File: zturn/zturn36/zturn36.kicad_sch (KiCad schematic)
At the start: 61 parts, among them J11 Conn_02x40_Odd_Even, J12 Conn_02x40_Odd_Even, J5V1 Conn_01x03, Q1 SSM6N15AFU, Q2 SSM6N15AFU, Q3 SSM6N15AFU, Q4 SSM6N15AFU, Q5 SSM6N15AFU, Q6 SSM6N15AFU, Q7 SSM6N15AFU, Q8 SSM6N15AFU, Q9 SSM6N15AFU, U1 74AXP4T245, U10 74AXP4T245, U11 74AXP4T245, U12 74AXP4T245, U13 74AXP4T245, U14 LM3940_TO220, U2 74AXP4T245, U3 74AXP4T245, U8 74AXP4T245, U9 74AXP4T245

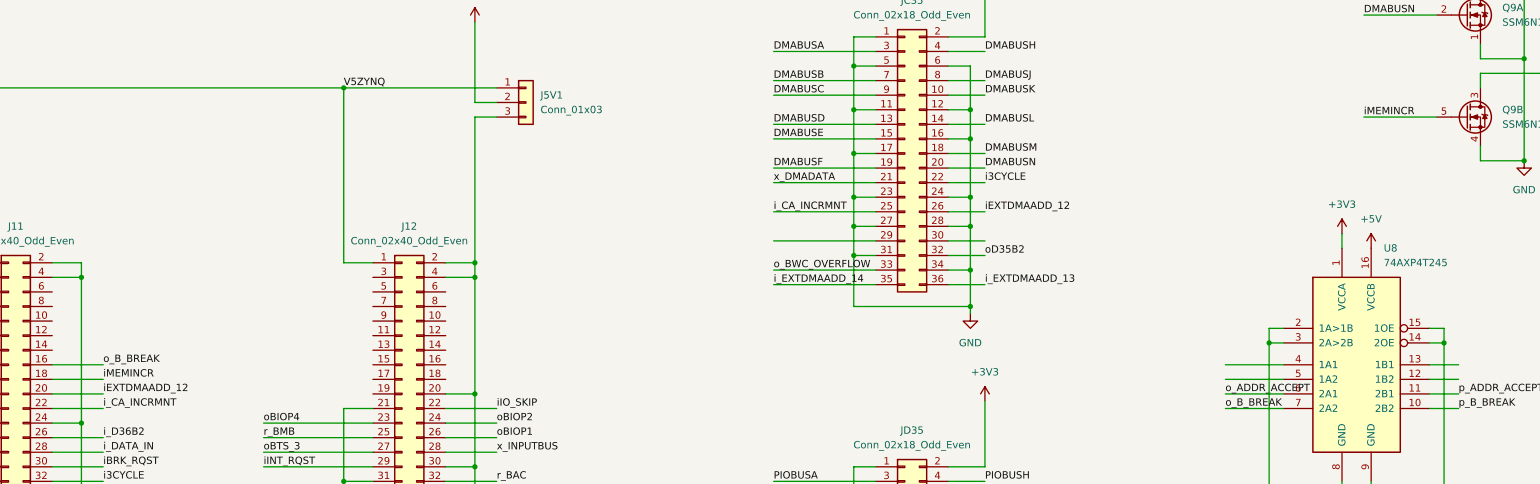
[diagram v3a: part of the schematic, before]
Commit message: fixed polarity of bus signals for the open-drain transistors
    PDP         Zynq
    MEM         _MEM
    MEM_P       _MEM_P
    _DMAADDR    DMAADDR
    _DMADATA    DMADATA
    _INPUTBUS   INPUTBUS

Also fixed MEMINCR polarity and fixed missing ground connection on circuit board.
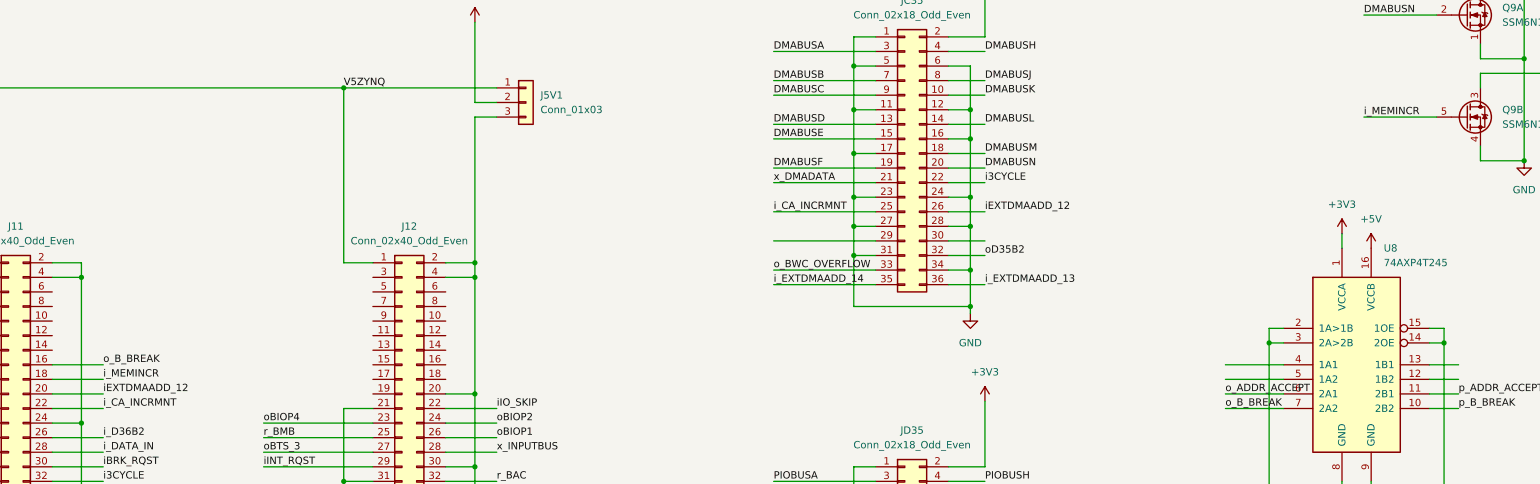
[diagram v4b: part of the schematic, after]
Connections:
- net iMEMINCR renamed i_MEMINCR
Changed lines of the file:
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@@
     (effects (font (size 1.27 1.27)) (justify left bottom))
   )
-  (label "iMEMINCR" (at 54.61 226.06 0) (fields_autoplaced)
+  (label "i_MEMINCR" (at 54.61 226.06 0) (fields_autoplaced)
     (effects (font (size 1.27 1.27)) (justify left bottom))
   )
@@
     (effects (font (size 1.27 1.27)) (justify left bottom))
   )
-  (label "iMEMINCR" (at 274.32 180.34 0) (fields_autoplaced)
+  (label "i_MEMINCR" (at 274.32 180.34 0) (fields_autoplaced)
     (effects (font (size 1.27 1.27)) (justify left bottom))
   )

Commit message: update signals and zturn pcbs with pullups
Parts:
- removed C4: 0.47u, Capacitor_SMD:C_0201_0603Metric, symbol Device:C
- removed C5: 33u, Capacitor_Tantalum_SMD:CP_EIA-7343-31_Kemet-D, symbol Device:C_Polarized_US
- removed U14: LM3940_TO220, Package_TO_SOT_THT:TO-220-3_Horizontal_TabDown, symbol Regulator_Linear:LM7805_TO220
- added R1, R2: 1K, Resistor_THT:R_Axial_DIN0204_L3.6mm_D1.6mm_P5.08mm_Horizontal, symbol Device:R_US
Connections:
- net +3V3: now also J11.3 (Pin_3), J12.3 (Pin_3)
- net +5V: now also R1.1, R2.1
- net jB36V1: now also R1.2
- net jD36B2: now also R2.2

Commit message: add I2C circuit to zturn boardset to operate front panel board
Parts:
- added JI2C1: Conn_01x03, Connector_PinHeader_2.54mm:PinHeader_1x03_P2.54mm_Horizontal, symbol Connector_Generic:Conn_01x03
- added R4: 1K, Resistor_THT:R_Axial_DIN0204_L3.6mm_D1.6mm_P5.08mm_Horizontal, symbol Device:R_US
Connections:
- net +3V3: now also U8.3 (2A>2B)
- net +5V: now also R4.1
- net GND: now also JI2C1.2 (Pin_2); no longer JC36.N2, U8.3 (2A>2B)
- net PIOBUSA: now also J11.27 (Pin_27); no longer J11.19 (Pin_19)
- net PIOBUSB: now also J11.31 (Pin_31); no longer J11.23 (Pin_23)
- net PIOBUSC: now also J11.37 (Pin_37); no longer J11.29 (Pin_29)
- net PIOBUSD: now also J12.36 (Pin_36); no longer J11.37 (Pin_37)
- net PIOBUSE: now also J12.34 (Pin_34); no longer J11.41 (Pin_41)
- net PIOBUSF: now also J12.26 (Pin_26); no longer J12.34 (Pin_34)
- net PIOBUSH: now also J11.29 (Pin_29); no longer J11.21 (Pin_21)
- net PIOBUSJ: now also J11.33 (Pin_33); no longer J11.27 (Pin_27)
- net PIOBUSK: now also J11.41 (Pin_41); no longer J11.31 (Pin_31)
- net PIOBUSL: now also J12.38 (Pin_38); no longer J11.33 (Pin_33)
- net PIOBUSM: now also J12.32 (Pin_32); no longer J12.38 (Pin_38)
- net PIOBUSN: now also J12.28 (Pin_28); no longer J12.36 (Pin_36)
- net iAC_CLEAR: now also J12.45 (Pin_45); no longer J12.35 (Pin_35)
- net iINT_RQST: now also J12.39 (Pin_39); no longer J12.29 (Pin_29)
- net iIO_SKIP: now also J12.29 (Pin_29); no longer J12.22 (Pin_22)
- net oBIOP1: now also J12.23 (Pin_23); no longer J12.26 (Pin_26)
- net oBIOP2: now also J12.27 (Pin_27); no longer J12.24 (Pin_24)
- net oBIOP4: now also J12.33 (Pin_33); no longer J12.23 (Pin_23)
- net oBTS_1: now also J12.43 (Pin_43); no longer J12.33 (Pin_33)
- net oBTS_3: now also J12.37 (Pin_37); no longer J12.27 (Pin_27)
- net oBUSINIT: now also J11.21 (Pin_21); no longer J11.13 (Pin_13)
- net oB_RUN: now also J12.47 (Pin_47); no longer J12.37 (Pin_37)
- net oC36B2: now also J11.23 (Pin_23); no longer J11.17 (Pin_17)
- net o_ADDR_ACCEPT: now also J11.19 (Pin_19), U8.4 (1A1); no longer J11.11 (Pin_11), U8.6 (2A1)
- net o_B_BREAK: now also J11.11 (Pin_11), U8.5 (1A2); no longer J11.16 (Pin_16), U8.7 (2A2)
- net p_ADDR_ACCEPT: now also U8.13 (1B1); no longer U8.11 (2B1)
- net p_B_BREAK: now also U8.12 (1B2); no longer U8.10 (2B2)
- net r_BAC: now also J12.24 (Pin_24); no longer J12.32 (Pin_32)
- net r_BMB: now also J12.35 (Pin_35); no longer J12.25 (Pin_25)
- net x_INPUTBUS: now also J12.22 (Pin_22); no longer J12.28 (Pin_28)
- net EPI2CDAT: now reaches JD35.22 (Pin_22)
- net EPI2CDAT: now also JI2C1.1 (Pin_1)
- net FPI2CDENA: now reaches JD35.25 (Pin_25)
- net FPI2CDENA: now also J12.25 (Pin_25)
- net i_EXTDMAADD_13 renamed FPI2CDATA
- net FPI2CDATA: now also J11.17 (Pin_17)
- net i_EXTDMAADD_14 renamed FPI2CDDIR
- net FPI2CDDIR: now also J11.13 (Pin_13)
- new net EPI2CCLK: JC36.N2, JI2C1.3 (Pin_3), R4.2, U8.11 (2B1)
- new net FPI2CCLK: J11.16 (Pin_16), U8.6 (2A1)

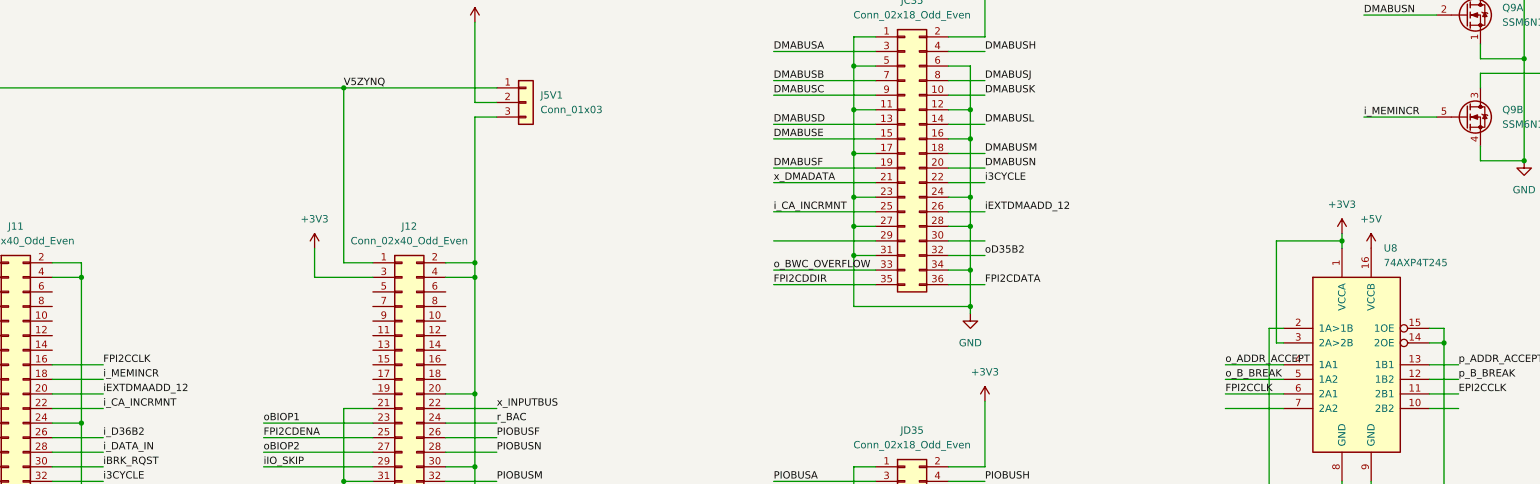
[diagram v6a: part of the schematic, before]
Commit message: fix hizmembus while reading memory and make iMEMINCR active high
at this point:
  looptest testrands works on core and fpga memory
  cmemtest works on fpga memory
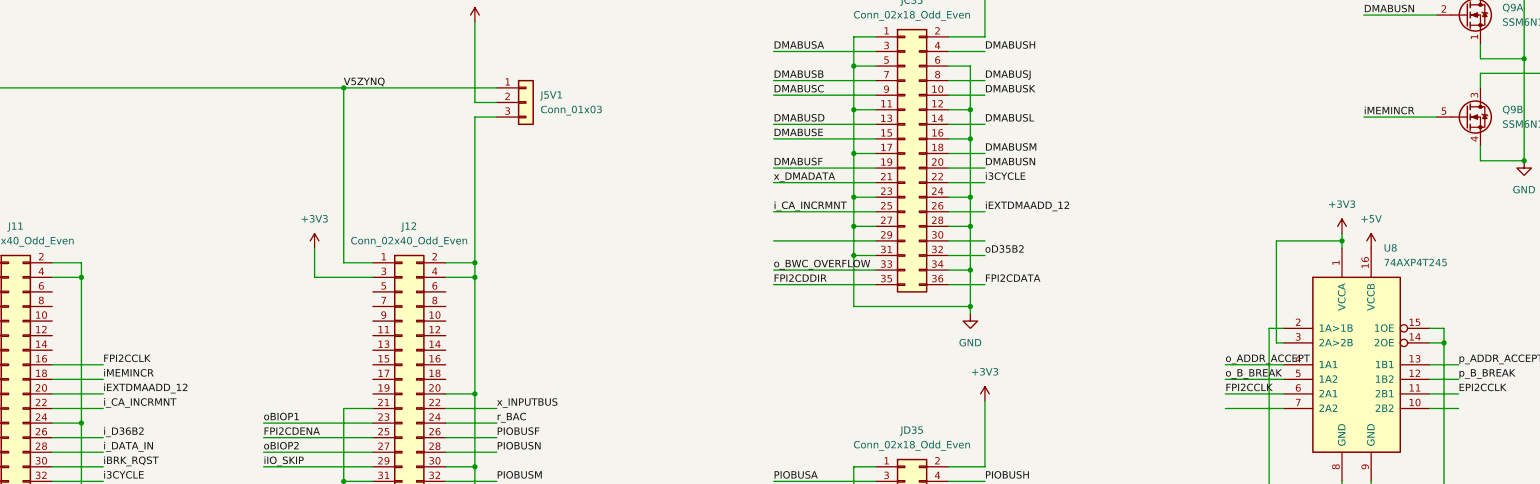
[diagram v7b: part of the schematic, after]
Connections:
- net i_MEMINCR renamed iMEMINCR
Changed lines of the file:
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@@
     (effects (font (size 1.27 1.27)) (justify left bottom))
   )
-  (label "i_MEMINCR" (at 54.61 226.06 0) (fields_autoplaced)
+  (label "iMEMINCR" (at 54.61 226.06 0) (fields_autoplaced)
     (effects (font (size 1.27 1.27)) (justify left bottom))
   )
@@
     (effects (font (size 1.27 1.27)) (justify left bottom))
   )
-  (label "i_MEMINCR" (at 274.32 180.34 0) (fields_autoplaced)
+  (label "iMEMINCR" (at 274.32 180.34 0) (fields_autoplaced)
     (effects (font (size 1.27 1.27)) (justify left bottom))
   )

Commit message: update zturn36,35 pcbs to put i2c at 3.3V and open-collector
...directly from FPGA pins with 2.2K pullups
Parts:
- added R5: 2.2K, Resistor_THT:R_Axial_DIN0204_L3.6mm_D1.6mm_P5.08mm_Horizontal, symbol Device:R_US
- R4: value 1K -> 2.2K
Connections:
- net +3V3: now also R4.1, R5.1
- net +5V: no longer R4.1
- net FPI2CCLK: now also JI2C1.3 (Pin_3), R4.2; no longer U8.6 (2A1)
- removed net EPI2CCLK: JC36.N2, JI2C1.3 (Pin_3), R4.2, U8.11 (2B1)
- net EPI2CDAT: no longer names the net of JD35.22 (Pin_22)
- net EPI2CDAT: no longer JI2C1.1 (Pin_1)
- net FPI2CDATA: no longer names the net of JC35.36 (Pin_36)
- net FPI2CDATA: no longer J11.17 (Pin_17)
- net FPI2CDDIR: no longer names the net of JC35.35 (Pin_35)
- net FPI2CDDIR: no longer J11.13 (Pin_13)
- net FPI2CDENA: no longer names the net of JD35.25 (Pin_25)
- net FPI2CDENA: no longer J12.25 (Pin_25)
- new net FPI2CDAT: J11.17 (Pin_17), JI2C1.1 (Pin_1), R5.2
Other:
- moved on the sheet: R4
